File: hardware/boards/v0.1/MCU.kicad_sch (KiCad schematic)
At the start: 37 parts, among them J1 LOGIC, SW24 NRST, SW25 BOOT0, U1 BMDU, U18 STM32H743ZIT6, Y1 ECS-.327-12.5-1210-TR, Y4 8Q-25.000MEEV-T

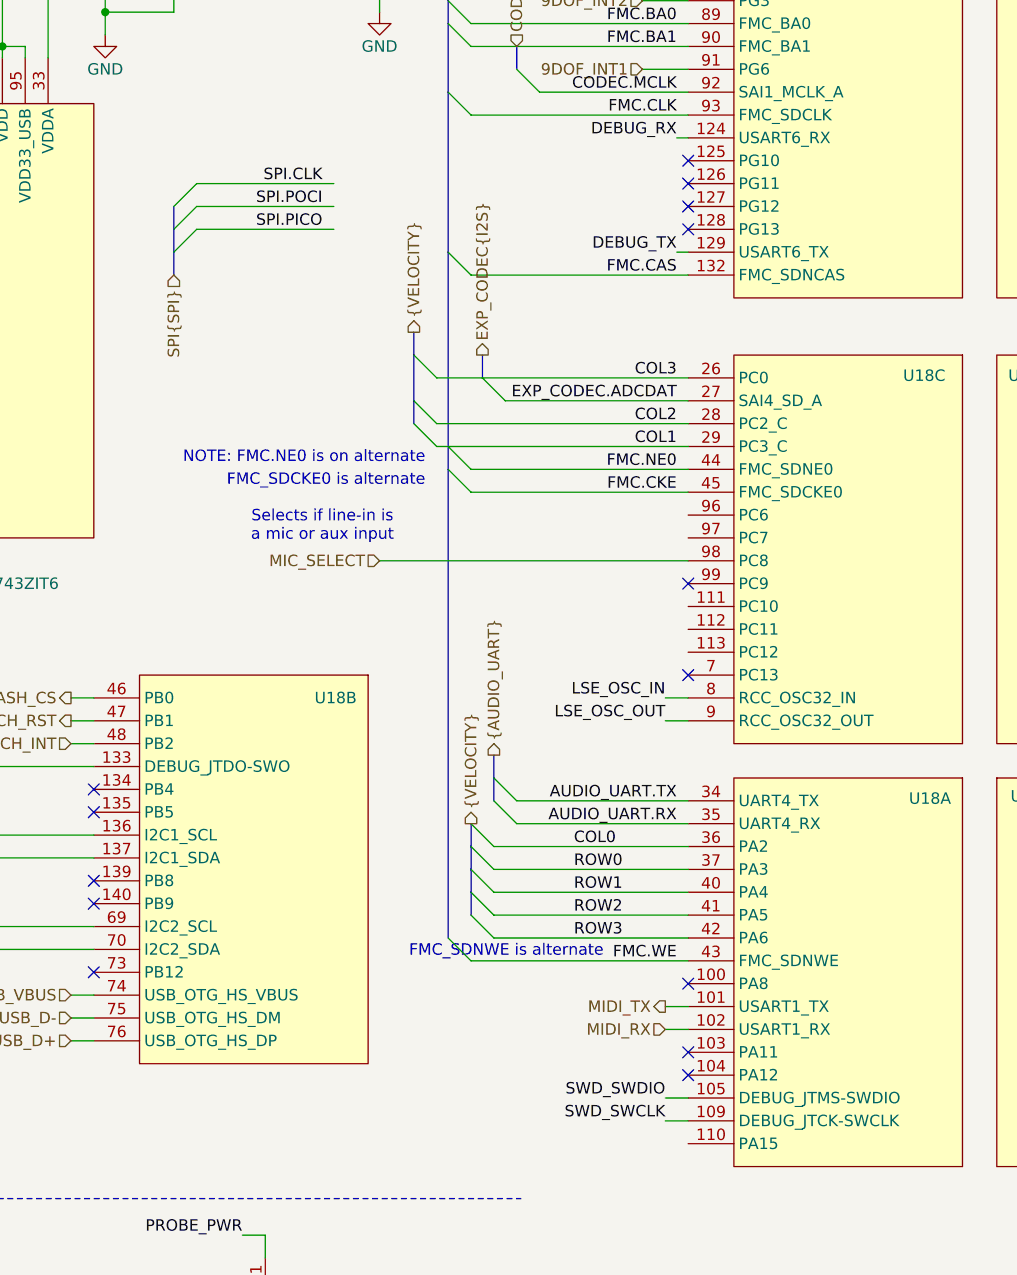
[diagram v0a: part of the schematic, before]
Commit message: feat: SD card SPI bus and routing
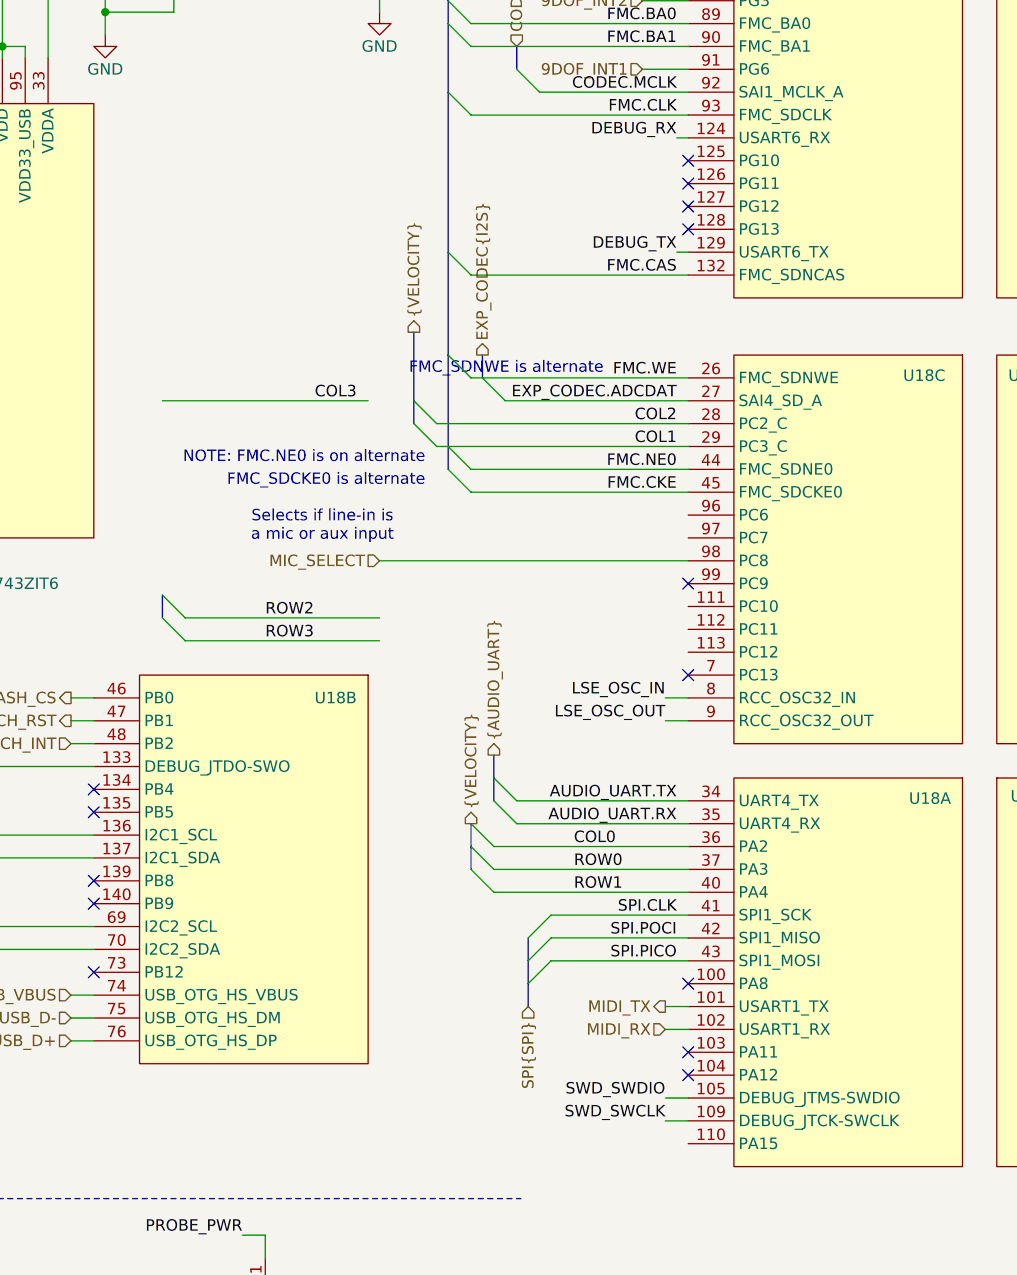
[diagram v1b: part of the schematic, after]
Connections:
- net COL3: no longer U18.26 (PC0)
- net FMC.WE: now also U18.26 (PC0); no longer U18.43 (PA7)
- net ROW2: no longer U18.41 (PA5)
- net ROW3: no longer U18.42 (PA6)
- net SPI.CLK: now also U18.41 (PA5)
- net SPI.PICO: now also U18.43 (PA7)
- net SPI.POCI: now also U18.42 (PA6)
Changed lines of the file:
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@@
 	(text "FMC_SDNWE is alternate\n"
 		(exclude_from_sim no)
-		(at 186.182 138.684 0)
+		(at 186.182 73.914 0)
 		(effects
 			(font
@@
 	)
 	(bus_entry
-		(at 140.97 53.34)
+		(at 180.34 134.62)
 		(size -2.54 2.54)
 		(stroke
@@
 	)
 	(bus_entry
-		(at 140.97 58.42)
+		(at 180.34 139.7)
 		(size -2.54 2.54)
 		(stroke
@@
 	)
 	(bus_entry
-		(at 171.45 139.7)
+		(at 171.45 74.93)
 		(size -2.54 -2.54)
 		(stroke
@@
 	)
 	(bus_entry
-		(at 140.97 55.88)
+		(at 180.34 137.16)
 		(size -2.54 2.54)
 		(stroke
@@
 	)
 	(bus_entry
-		(at 173.99 137.16)
+		(at 139.7 104.14)
 		(size -2.54 -2.54)
 		(stroke
@@
 	)
 	(bus_entry
-		(at 173.99 134.62)
+		(at 139.7 101.6)
 		(size -2.54 -2.54)
 		(stroke
@@
 	)
 	(bus_entry
-		(at 167.64 74.93)
-		(size -2.54 -2.54)
-		(stroke
-			(width 0)
-			(type default)
-		)
-	)
-	(bus_entry
 		(at 273.05 87.63)
 		(size 2.54 -2.54)
@@
 	(wire
 		(pts
-			(xy 173.99 134.62) (xy 195.58 134.62)
+			(xy 139.7 101.6) (xy 161.29 101.6)
 		)
 		(stroke
@@
 	(wire
 		(pts
-			(xy 140.97 55.88) (xy 156.21 55.88)
+			(xy 180.34 137.16) (xy 195.58 137.16)
 		)
 		(stroke
@@
 	(wire
 		(pts
-			(xy 167.64 74.93) (xy 172.72 74.93)
-		)
-		(stroke
-			(width 0)
-			(type default)
-		)
-	)
-	(wire
-		(pts
 			(xy 130.81 19.05) (xy 130.81 21.59)
 		)
@@
 	(bus
 		(pts
-			(xy 138.43 58.42) (xy 138.43 55.88)
+			(xy 177.8 139.7) (xy 177.8 137.16)
 		)
 		(stroke
@@
 	(bus
 		(pts
-			(xy 138.43 60.96) (xy 138.43 58.42)
+			(xy 177.8 142.24) (xy 177.8 139.7)
 		)
 		(stroke
@@
 	(wire
 		(pts
+			(xy 172.72 74.93) (xy 195.58 74.93)
+		)
+		(stroke
+			(width 0)
+			(type default)
+		)
+	)
+	(wire
+		(pts
 			(xy 26.67 21.59) (xy 34.29 21.59)
 		)
@@
 	(bus
 		(pts
-			(xy 168.91 60.96) (xy 168.91 82.55)
+			(xy 168.91 60.96) (xy 168.91 72.39)
 		)
 		(stroke
@@
 	(wire
 		(pts
-			(xy 171.45 139.7) (xy 195.58 139.7)
+			(xy 171.45 74.93) (xy 172.72 74.93)
 		)
 		(stroke
@@
 	(bus
 		(pts
+			(xy 168.91 72.39) (xy 168.91 82.55)
+		)
+		(stroke
+			(width 0)
+			(type default)
+		)
+	)
+	(bus
+		(pts
 			(xy 279.4 144.78) (xy 279.4 147.32)
 		)
@@
 	(bus
 		(pts
-			(xy 168.91 85.09) (xy 168.91 137.16)
-		)
-		(stroke
-			(width 0)
-			(type default)
-		)
-	)
-	(bus
-		(pts
 			(xy 275.59 43.18) (xy 275.59 45.72)
 		)
@@
 	(wire
 		(pts
-			(xy 140.97 53.34) (xy 156.21 53.34)
+			(xy 180.34 134.62) (xy 195.58 134.62)
 		)
 		(stroke
@@
 	(wire
 		(pts
-			(xy 173.99 137.16) (xy 195.58 137.16)
+			(xy 139.7 104.14) (xy 161.29 104.14)
 		)
 		(stroke
@@
 	(bus
 		(pts
-			(xy 165.1 69.85) (xy 165.1 72.39)
+			(xy 165.1 69.85) (xy 165.1 77.47)
 		)
 		(stroke
@@
 		)
 	)
-	(bus
-		(pts
-			(xy 171.45 129.54) (xy 171.45 132.08)
-		)
-		(stroke
-			(width 0)
-			(type default)
-		)
-	)
 	(wire
 		(pts
@@
 	(bus
 		(pts
-			(xy 171.45 132.08) (xy 171.45 134.62)
+			(xy 137.16 99.06) (xy 137.16 101.6)
 		)
 		(stroke
@@
 	(wire
 		(pts
-			(xy 172.72 74.93) (xy 195.58 74.93)
+			(xy 137.16 77.47) (xy 160.02 77.47)
 		)
 		(stroke
@@
 	(bus
 		(pts
-			(xy 138.43 63.5) (xy 138.43 60.96)
+			(xy 177.8 144.78) (xy 177.8 142.24)
 		)
 		(stroke
@@
 		)
 	)
-	(bus
-		(pts
-			(xy 165.1 72.39) (xy 165.1 77.47)
-		)
-		(stroke
-			(width 0)
-			(type default)
-		)
-	)
 	(wire
 		(pts
@@
 	(wire
 		(pts
-			(xy 140.97 58.42) (xy 156.21 58.42)
+			(xy 180.34 139.7) (xy 195.58 139.7)
 		)
 		(stroke
@@
 	)
 	(label "ROW3"
-		(at 182.88 137.16 0)
+		(at 148.59 104.14 0)
 		(effects
 			(font
@@
 	)
 	(label "ROW2"
-		(at 182.88 134.62 0)
+		(at 148.59 101.6 0)
 		(effects
 			(font
@@
 	)
 	(label "FMC.WE"
-		(at 194.31 139.7 180)
+		(at 194.31 74.93 180)
 		(effects
 			(font
@@
 	)
 	(label "COL3"
-		(at 194.31 74.93 180)
+		(at 158.75 77.47 180)
 		(effects
 			(font
@@
 	)
 	(label "SPI.POCI"
-		(at 154.94 55.88 180)
+		(at 194.31 137.16 180)
 		(effects
 			(font
@@
 	)
 	(label "SPI.CLK"
-		(at 154.94 53.34 180)
+		(at 194.31 134.62 180)
 		(effects
 			(font
@@
 	)
 	(label "SPI.PICO"
-		(at 154.94 58.42 180)
+		(at 194.31 139.7 180)
 		(effects
 			(font
@@
 	(hierarchical_label "SPI{SPI}"
 		(shape input)
-		(at 138.43 63.5 270)
+		(at 177.8 144.78 270)
 		(effects
 			(font
@@
 		)
 		(pin "41"
+			(alternate "SPI1_SCK")
 		)
 		(pin "42"
+			(alternate "SPI1_MISO")
 		)
 		(pin "43"
-			(alternate "FMC_SDNWE")
+			(alternate "SPI1_MOSI")
 		)
 		(pin "100"
@@
 		)
 		(pin "26"
+			(alternate "FMC_SDNWE")
 		)
 		(pin "27"

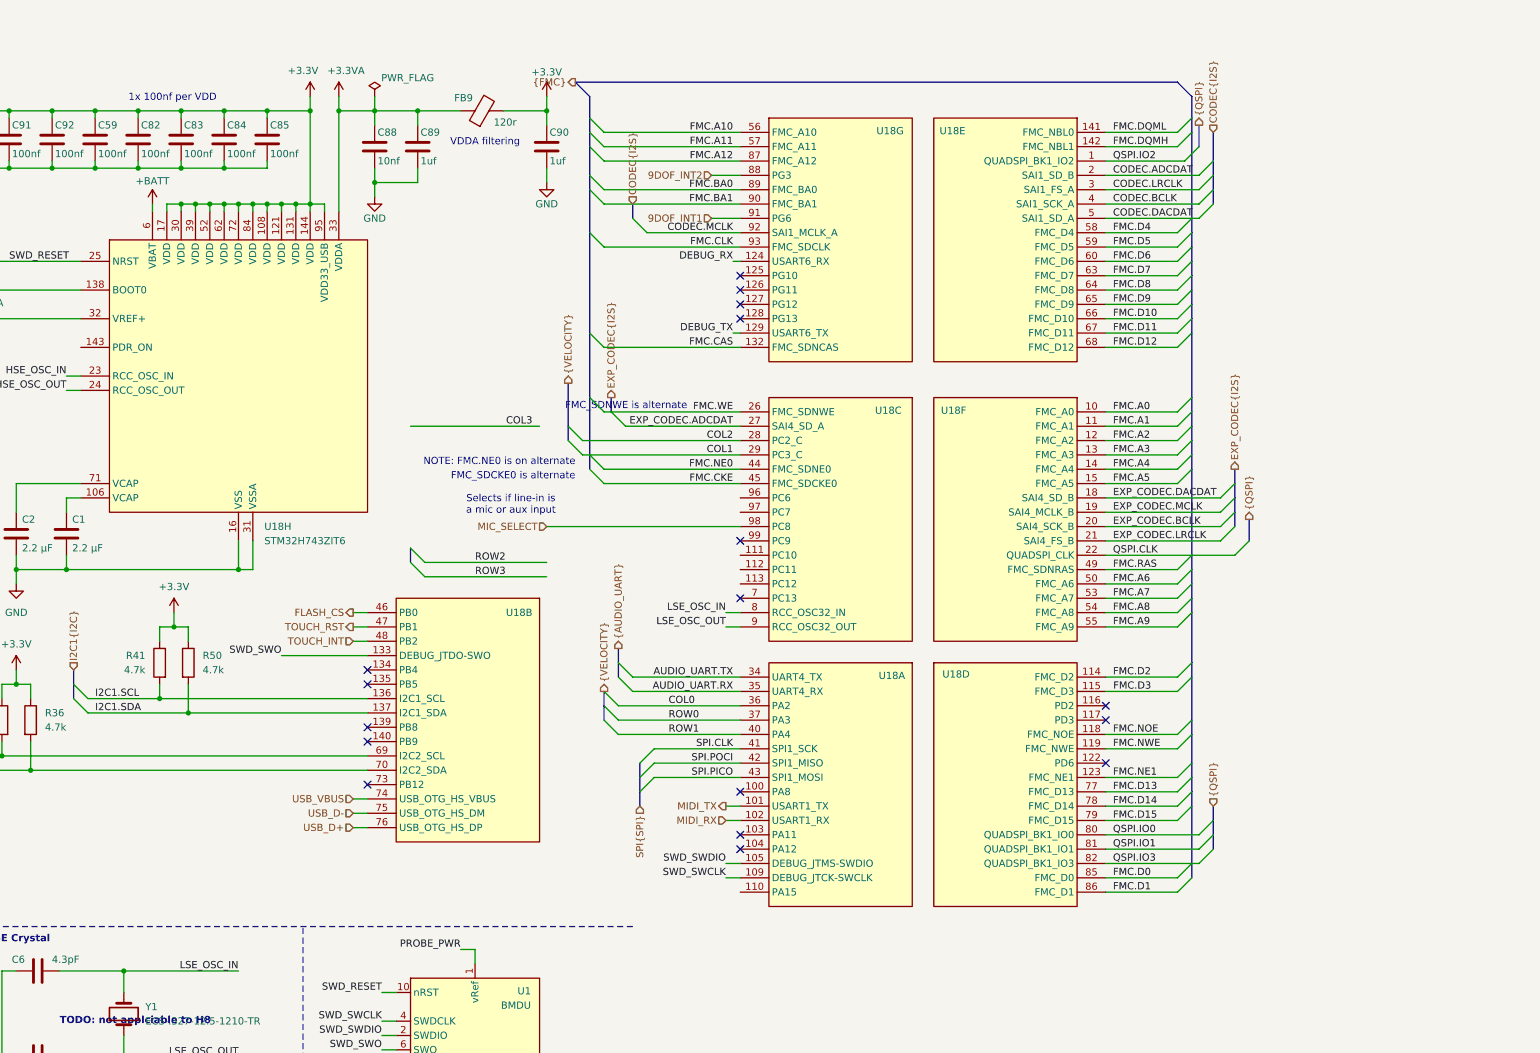
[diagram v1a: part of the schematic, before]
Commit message: feat: various routing and organization
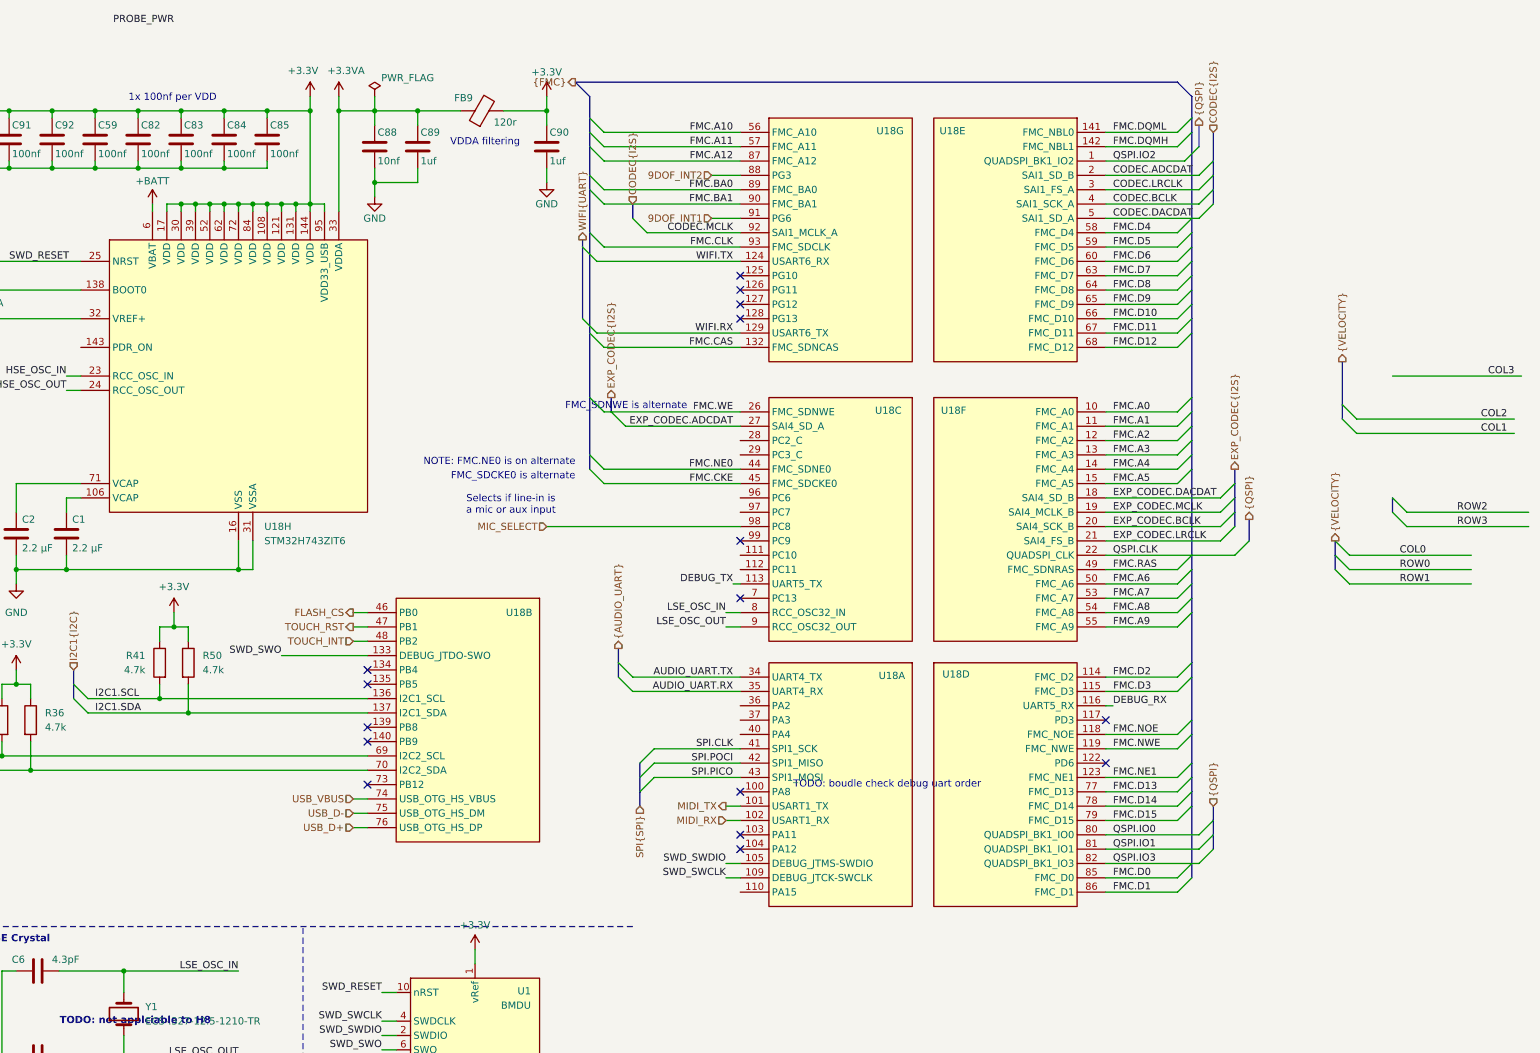
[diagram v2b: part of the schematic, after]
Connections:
- net +3.3V: now also U1.1 (vRef)
- net COL0: no longer U18.36 (PA2)
- net COL1: no longer U18.29 (PC3_C)
- net COL2: no longer U18.28 (PC2_C)
- net DEBUG_RX: now also U18.116 (PD2); no longer U18.124 (PG9)
- net DEBUG_TX: now also U18.113 (PC12); no longer U18.129 (PG14)
- net PROBE_PWR: no longer U1.1 (vRef)
- net ROW0: no longer U18.37 (PA3)
- net ROW1: no longer U18.40 (PA4)
- new net WIFI.RX: U18.129 (PG14)
- new net WIFI.TX: U18.124 (PG9)
- no-connect marks 17 -> 16
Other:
- note added: "TODO: boudle check debug uart order"

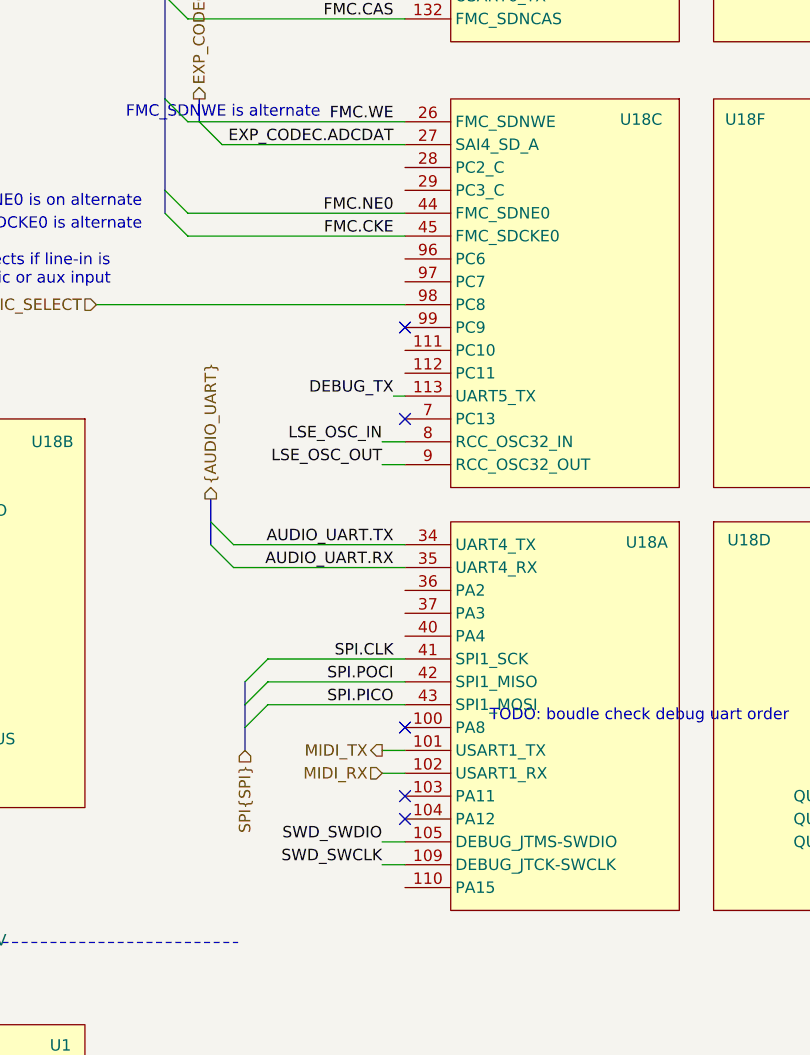
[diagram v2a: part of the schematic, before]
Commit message: feat: schematic organization and ERC cleanup
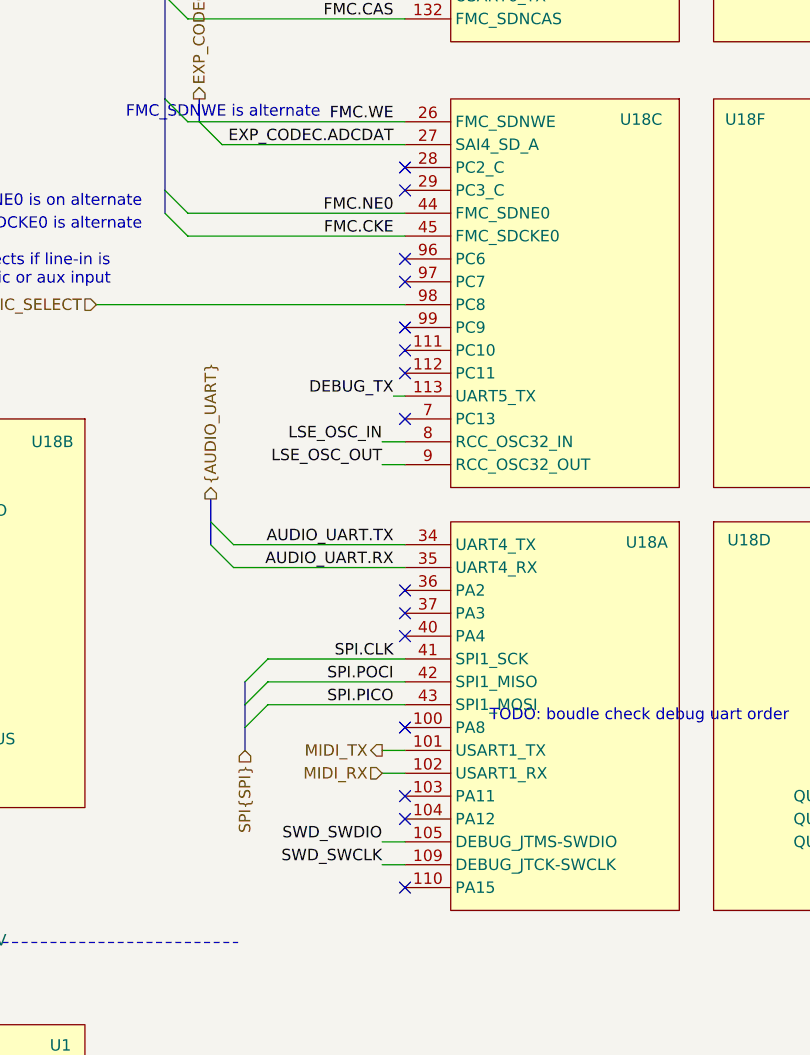
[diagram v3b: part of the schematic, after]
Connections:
- no-connect marks 16 -> 26
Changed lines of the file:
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@@
+	)
+	(no_connect
+		(at 195.58 90.17)
 	)
 	(no_connect
 		(at 195.58 142.24)
+	)
+	(no_connect
+		(at 195.58 80.01)
 	)
 	(no_connect
@@
 	)
 	(no_connect
+		(at 195.58 102.87)
+	)
+	(no_connect
 		(at 129.54 130.81)
+	)
+	(no_connect
+		(at 195.58 92.71)
 	)
 	(no_connect
@@
 	)
 	(no_connect
+		(at 195.58 82.55)
+	)
+	(no_connect
+		(at 195.58 160.02)
+	)
+	(no_connect
 		(at 129.54 120.65)
 	)
 	(no_connect
 		(at 260.35 129.54)
+	)
+	(no_connect
+		(at 195.58 129.54)
+	)
+	(no_connect
+		(at 195.58 132.08)
 	)
 	(no_connect
@@
 	)
 	(no_connect
+		(at 195.58 100.33)
+	)
+	(no_connect
 		(at 129.54 133.35)
 	)
 	(no_connect
+		(at 195.58 127)
+	)
+	(no_connect
